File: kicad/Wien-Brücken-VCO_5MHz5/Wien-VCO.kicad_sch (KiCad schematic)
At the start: 22 parts, among them J1 J113, U1 ${SIM.NAME}

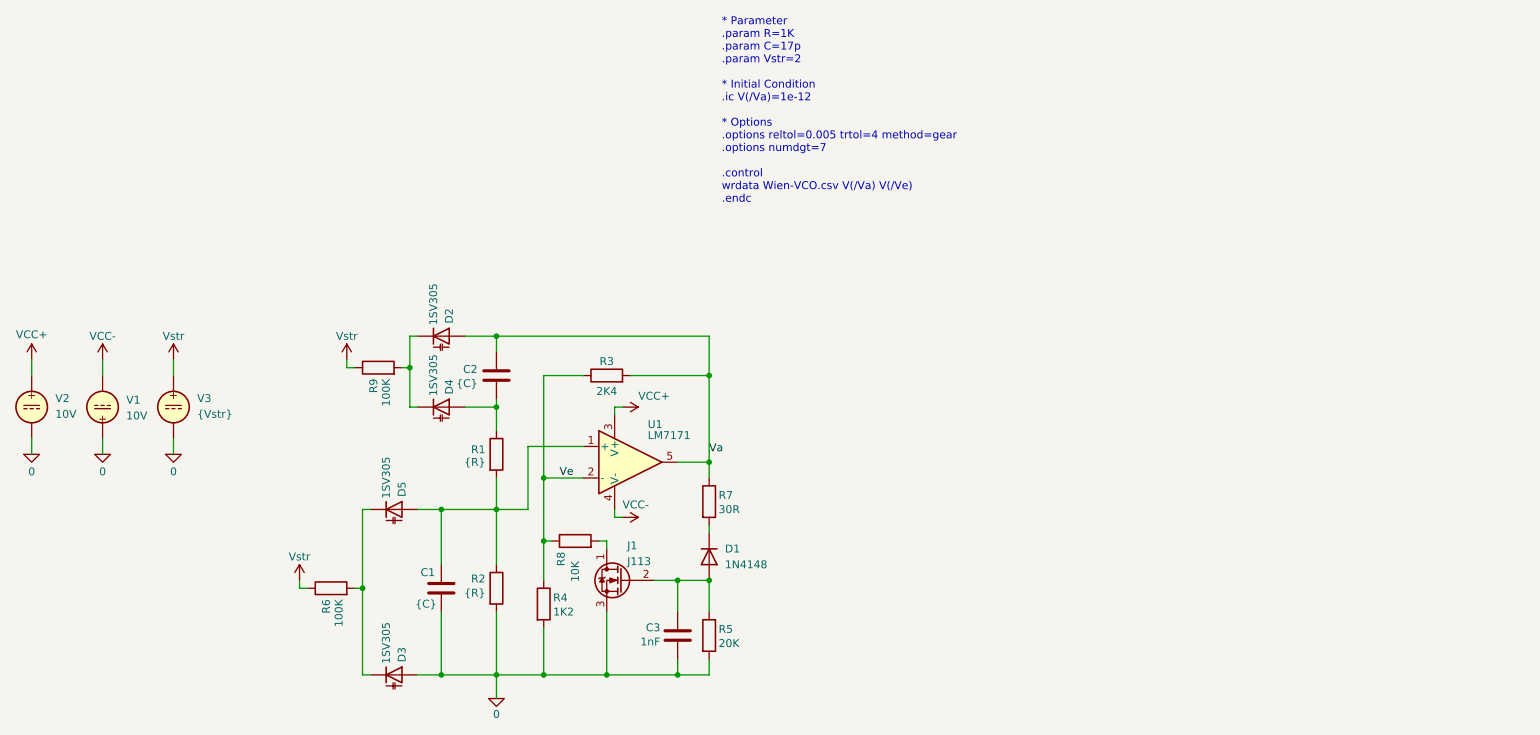
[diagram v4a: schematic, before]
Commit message: Schaltung in LTSpice angepasst
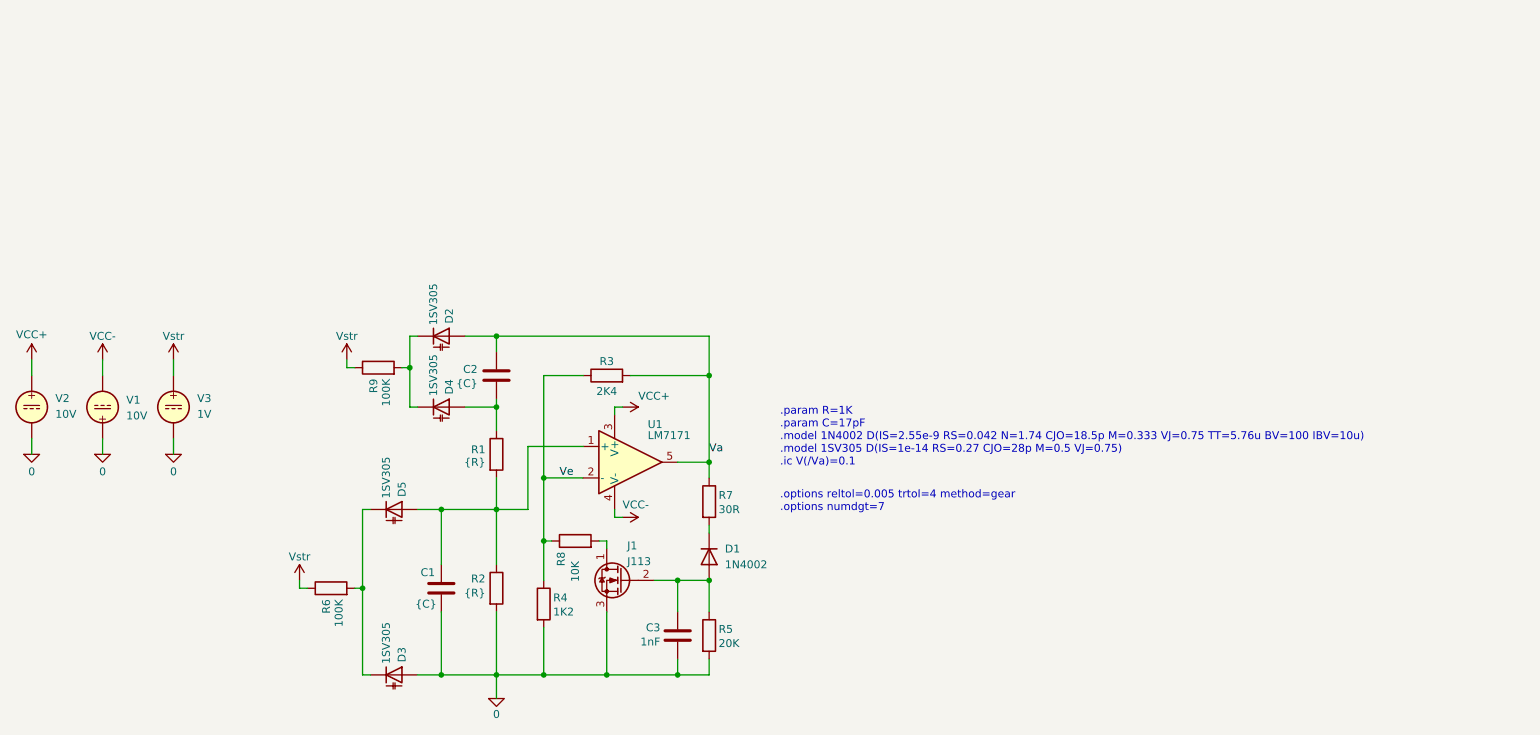
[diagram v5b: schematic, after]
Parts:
- D1: value 1N4148 -> 1N4002
- V3: value {Vstr} -> 1V
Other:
- note added: ".options reltol=0.005 trtol=4 method=gear .options numdgt=7"
- note added: ".param R=1K .param C=17pF .model 1N4002 D(IS=2.55e-9 RS=0.042 N=1.74 CJO=18.5p M=0.333 VJ=0.75 TT=5.76u BV=100 IBV=10u) .model 1SV305 D(IS=1e-14 RS=0.27 CJO=28p M=0.5 VJ=0.75) .ic V(/Va)=0.1"
- note removed: "* Parameter .param R=1K .param C=17p .param Vstr=2 * Initial Condition .ic V(/Va)=1e-12 * Options .options reltol=0.005 trtol=4 method=gear .options numdgt=7 .control wrdata Wien-VCO.csv V(/Va) V(/Ve) .endc"
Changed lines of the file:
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@@
 	(generator_version "10.0")
 	(paper "A4")
-	(text "* Parameter\n.param R=1K\n.param C=17p\n.param Vstr=2\n\n* Initial Condition\n.ic V(/Va)=1e-12\n\n* Options\n.options reltol=0.005 trtol=4 method=gear\n.options numdgt=7\n\n.control\nwrdata Wien-VCO.csv V(/Va) V(/Ve)\n.endc"
+	(text ".param R=1K\n.param C=17pF\n.model 1N4002 D(IS=2.55e-9 RS=0.042 N=1.74 CJO=18.5p M=0.333 VJ=0.75 TT=5.76u BV=100 IBV=10u)\n.model 1SV305 D(IS=1e-14 RS=0.27 CJO=28p M=0.5 VJ=0.75)\n.ic V(/Va)=0.1"
 		(exclude_from_sim no)
-		(at 159.512 41.148 0)
+		(at 168.91 93.726 0)
 		(effects
 			(font
@@
 		)
 	)
-	(text ""
+	(text ".options reltol=0.005 trtol=4 method=gear\n.options numdgt=7"
 		(exclude_from_sim yes)
 		(at 168.91 104.14 0)
@@
 	)
 	(junction
-		(at 157.48 97.79)
+		(at 157.48 116.84)
 		(diameter 0)
 		(color 0 0 0 0)
 	)
 	(junction
-		(at 130.81 100.33)
+		(at 157.48 97.79)
 		(diameter 0)
 		(color 0 0 0 0)
 	)
 	(junction
-		(at 109.22 82.55)
+		(at 130.81 100.33)
 		(diameter 0)
 		(color 0 0 0 0)
 	)
 	(junction
-		(at 157.48 116.84)
+		(at 109.22 82.55)
 		(diameter 0)
 		(color 0 0 0 0)
@@
 			)
 		)
-		(property "Sim.Library" "../spicelibs/lm7171.lib"
+		(property "Sim.Library" "..\\spicelibs\\lm7171.lib"
 			(at 144.78 97.79 0)
 			(hide yes)
@@
 	)
 	(symbol
-		(lib_id "Diode:1N4148")
-		(at 157.48 113.03 270)
-		(unit 1)
-		(body_style 1)
-		(exclude_from_sim no)
-		(in_bom yes)
-		(on_board yes)
-		(in_pos_files yes)
-		(dnp no)
-		(fields_autoplaced yes)
-		(property "Reference" "D1"
-			(at 160.02 111.7599 90)
-			(show_name no)
-			(do_not_autoplace no)
-			(effects
-				(font
-					(size 1.27 1.27)
-				)
-				(justify left)
-			)
-		)
-		(property "Value" "1N4148"
-			(at 160.02 114.2999 90)
-			(show_name no)
-			(do_not_autoplace no)
-			(effects
-				(font
-					(size 1.27 1.27)
-				)
-				(justify left)
-			)
-		)
-		(property "Footprint" "Diode_THT:D_DO-35_SOD27_P7.62mm_Horizontal"
-			(at 157.48 113.03 0)
-			(hide yes)
-			(show_name no)
-			(do_not_autoplace no)
-			(effects
-				(font
-					(size 1.27 1.27)
-				)
-			)
-		)
-		(property "Datasheet" "https://assets.nexperia.com/documents/data-sheet/1N4148_1N4448.pdf"
-			(at 157.48 113.03 0)
-			(hide yes)
-			(show_name no)
-			(do_not_autoplace no)
-			(effects
-				(font
-					(size 1.27 1.27)
-				)
-			)
-		)
-		(property "Description" "100V 0.15A standard switching diode, DO-35"
-			(at 157.48 113.03 0)
-			(hide yes)
-			(show_name no)
-			(do_not_autoplace no)
-			(effects
-				(font
-					(size 1.27 1.27)
-				)
-			)
-		)
-		(property "Sim.Device" "D"
-			(at 157.48 113.03 0)
-			(hide yes)
-			(show_name no)
-			(do_not_autoplace no)
-			(effects
-				(font
-					(size 1.27 1.27)
-				)
-			)
-		)
-		(property "Sim.Pins" "1=K 2=A"
-			(at 157.48 113.03 0)
-			(hide yes)
-			(show_name no)
-			(do_not_autoplace no)
-			(effects
-				(font
-					(size 1.27 1.27)
-				)
-			)
-		)
-		(property "Sim.Library" "../spicelibs/elk.lib"
-			(at 157.48 113.03 0)
-			(hide yes)
-			(show_name no)
-			(do_not_autoplace no)
-			(effects
-				(font
-					(size 1.27 1.27)
-				)
-			)
-		)
-		(property "Sim.Name" "D1N4148"
-			(at 157.48 113.03 0)
-			(hide yes)
-			(show_name no)
-			(do_not_autoplace no)
-			(effects
-				(font
-					(size 1.27 1.27)
-				)
-			)
-		)
-		(pin "1"
-		)
-		(pin "2"
-		)
-		(instances
-			(project "Wien-VCO"
-				(path "/61a7698a-1c0d-4258-9661-7a52612acc47"
-					(reference "D1")
-					(unit 1)
-				)
-			)
-		)
-	)
-	(symbol
 		(lib_id "Device:R")
 		(at 123.19 96.52 0)
@@
 	)
 	(symbol
-		(lib_id "Device:D_Capacitance")
-		(at 114.3 88.9 0)
+		(lib_id "Diode:1N4148")
+		(at 157.48 113.03 270)
 		(unit 1)
 		(body_style 1)
@@
 		(in_pos_files yes)
 		(dnp no)
-		(property "Reference" "D4"
-			(at 115.57 86.868 90)
+		(fields_autoplaced yes)
+		(property "Reference" "D1"
+			(at 160.02 111.7599 90)
 			(show_name no)
 			(do_not_autoplace no)
@@
 			)
 		)
-		(property "Value" "1SV305"
-			(at 113.03 87.122 90)
+		(property "Value" "1N4002"
+			(at 160.02 114.2999 90)
 			(show_name no)
 			(do_not_autoplace no)
@@
 			)
 		)
-		(property "Footprint" ""
-			(at 114.3 88.9 0)
+		(property "Footprint" "Diode_THT:D_DO-35_SOD27_P7.62mm_Horizontal"
+			(at 157.48 113.03 0)
 			(hide yes)
 			(show_name no)
@@
 			)
 		)
-		(property "Datasheet" ""
-			(at 114.3 88.9 0)
+		(property "Datasheet" "https://assets.nexperia.com/documents/data-sheet/1N4148_1N4448.pdf"
+			(at 157.48 113.03 0)
 			(hide yes)
 			(show_name no)
@@
 			)
 		)
-		(property "Description" "Variable capacitance diode"
+		(property "Description" "100V 0.15A standard switching diode, DO-35"
+			(at 157.48 113.03 0)
+			(hide yes)
+			(show_name no)
+			(do_not_autoplace no)
+			(effects
+				(font
+					(size 1.27 1.27)
+				)
+			)
+		)
+		(property "Sim.Device" "1N4002"
+			(at 157.48 113.03 0)
+			(hide yes)
+			(show_name no)
+			(do_not_autoplace no)
+			(effects
+				(font
+					(size 1.27 1.27)
+				)
+			)
+		)
+		(property "Sim.Pins" "1=K 2=A"
+			(at 157.48 113.03 0)
+			(hide yes)
+			(show_name no)
+			(do_not_autoplace no)
+			(effects
+				(font
+					(size 1.27 1.27)
+				)
+			)
+		)
+		(pin "2"
+		)
+		(pin "1"
+		)
+		(instances
+			(project "Wien-VCO"
+				(path "/61a7698a-1c0d-4258-9661-7a52612acc47"
+					(reference "D1")
+					(unit 1)
+				)
+			)
+		)
+	)
+	(symbol
+		(lib_id "Device:D_Capacitance")
+		(at 114.3 88.9 0)
+		(unit 1)
+		(body_style 1)
+		(exclude_from_sim no)
+		(in_bom yes)
+		(on_board yes)
+		(in_pos_files yes)
+		(dnp no)
+		(property "Reference" "D4"
+			(at 115.57 86.868 90)
+			(show_name no)
+			(do_not_autoplace no)
+			(effects
+				(font
+					(size 1.27 1.27)
+				)
+				(justify left)
+			)
+		)
+		(property "Value" "1SV305"
+			(at 113.03 87.122 90)
+			(show_name no)
+			(do_not_autoplace no)
+			(effects
+				(font
+					(size 1.27 1.27)
+				)
+				(justify left)
+			)
+		)
+		(property "Footprint" ""
 			(at 114.3 88.9 0)
 			(hide yes)
@@
 			)
 		)
-		(property "Sim.Device" "D"
+		(property "Datasheet" ""
 			(at 114.3 88.9 0)
 			(hide yes)
@@
 			)
 		)
-		(property "Sim.Pins" "1=K 2=A"
+		(property "Description" "Variable capacitance diode"
 			(at 114.3 88.9 0)
 			(hide yes)
@@
 			)
 		)
-		(property "Sim.Library" "../spicelibs/elk.lib"
+		(property "Sim.Device" "1SV305"
 			(at 114.3 88.9 0)
 			(hide yes)
@@
 			)
 		)
-		(property "Sim.Name" "1SV305"
+		(property "Sim.Pins" "1=K 2=A"
 			(at 114.3 88.9 0)
 			(hide yes)
@@
 			)
 		)
-		(property "Sim.Device" "D"
+		(property "Sim.Device" "1SV305"
 			(at 114.3 77.47 0)
 			(hide yes)
@@
 			)
 		)
-		(property "Sim.Library" "../spicelibs/elk.lib"
-			(at 114.3 77.47 0)
-			(hide yes)
-			(show_name no)
-			(do_not_autoplace no)
-			(effects
-				(font
-					(size 1.27 1.27)
-				)
-			)
-		)
-		(property "Sim.Name" "1SV305"
-			(at 114.3 77.47 0)
-			(hide yes)
-			(show_name no)
-			(do_not_autoplace no)
-			(effects
-				(font
-					(size 1.27 1.27)
-				)
-			)
-		)
 		(pin "2"
 		)
@@
 			)
 		)
-		(property "Sim.Device" "D"
+		(property "Sim.Device" "1SV305"
 			(at 106.68 105.41 0)
 			(hide yes)
@@
 			)
 		)
-		(property "Sim.Library" "../spicelibs/elk.lib"
-			(at 106.68 105.41 0)
-			(hide yes)
-			(show_name no)
-			(do_not_autoplace no)
-			(effects
-				(font
-					(size 1.27 1.27)
-				)
-			)
-		)
-		(property "Sim.Name" "1SV305"
-			(at 106.68 105.41 0)
-			(hide yes)
-			(show_name no)
-			(do_not_autoplace no)
-			(effects
-				(font
-					(size 1.27 1.27)
-				)
-			)
-		)
 		(pin "2"
 		)
@@
 			)
 		)
-		(property "Sim.Library" "../spicelibs/J113.lib"
+		(property "Sim.Library" "..\\spicelibs\\MeinJ113.lib"
 			(at 143.51 116.84 0)
 			(hide yes)
@@
 			)
 		)
-		(property "Sim.Name" "J113"
+		(property "Sim.Name" "MeinJ113"
 			(at 143.51 116.84 0)
 			(hide yes)
@@
 			)
 		)
-		(property "Value" "{Vstr}"
+		(property "Value" "1V"
 			(at 74.93 90.0401 0)
 			(show_name no)
@@
 			)
 		)
-		(property "Sim.Device" "D"
+		(property "Sim.Device" "1SV305"
 			(at 106.68 132.08 0)
 			(hide yes)
@@
 			(at 106.68 132.08 0)
 			(hide yes)
-			(show_name no)
-			(do_not_autoplace no)
-			(effects
-				(font
-					(size 1.27 1.27)
-				)
-			)
-		)
-		(property "Sim.Library" "../spicelibs/elk.lib"
-			(at 106.68 132.08 0)
-			(hide yes)
-			(show_name no)
-			(do_not_autoplace no)
-			(effects
-				(font
-					(size 1.27 1.27)
-				)
-			)
-		)
-		(property "Sim.Name" "1SV305"
-			(at 106.68 132.08 0)
-			(hide yes)
